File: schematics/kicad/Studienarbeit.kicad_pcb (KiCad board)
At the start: 2 copper layers, 73 x 73 mm, 84 parts, among them J2 Conn_01x18, J3 Conn_01x18, J4 Conn_01x01_Pin, J5 Conn_01x01_Pin, J6 Conn_01x01_Pin, J7 Conn_01x01_Pin, J9 SJ2-35853B-SMT-TR, U2 PCM5102, U3 MCP6001-OT, U4 MCP6001-OT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

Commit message: Last board updates before ordering.
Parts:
- removed CC_TPA711: 330uF, Capacitor_SMD:C_1206_3216Metric_Pad1.33x1.80mm_HandSolder
- added C_INPUT_TPA3: 10uF, Capacitor_SMD:C_1206_3216Metric_Pad1.33x1.80mm_HandSolder, F.Cu at (266.1, 77.5)
- C2_CPPS_PCM1, CA_PCM5102, CB_TPA1: footprint Capacitor_SMD:C_0805_2012Metric_Pad1.18x1.45mm_HandSolder -> Capacitor_SMD:C_1206_3216Metric_Pad1.33x1.80mm_HandSolder
- moved C1_CPPS_PCM1 1.17 mm to (235.8, 102.2)
- moved C2_CPPS_PCM1 0.88 mm to (230.4, 102.3)
- moved C1_DPS_PCM1 0.63 mm to (225.4, 101.5)
- moved C2_DPS_PCM1 0.60 mm to (221.8, 101.2)
- moved CG1_PCM5102 0.59 mm to (236.9, 89.2)
- moved CG2_PCM5102 0.59 mm to (234.6, 89.2)
- moved ROUTDACL1 0.59 mm to (236.9, 93.6)
- moved ROUTDACR1 0.59 mm to (234.6, 93.5)
- moved CB_TPA1 0.48 mm to (253.0, 70.2)
- moved C_SE/BTL_TPA1 0.40 mm to (254.2, 74.0)
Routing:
- net GND: track 90.4 -> 87.5 mm
- net +5V: track 247.2 -> 250.2 mm
- net /Vo+: track 25.6 -> 27.0 mm
- net /VNEG: track 5.05 -> 6.36 mm

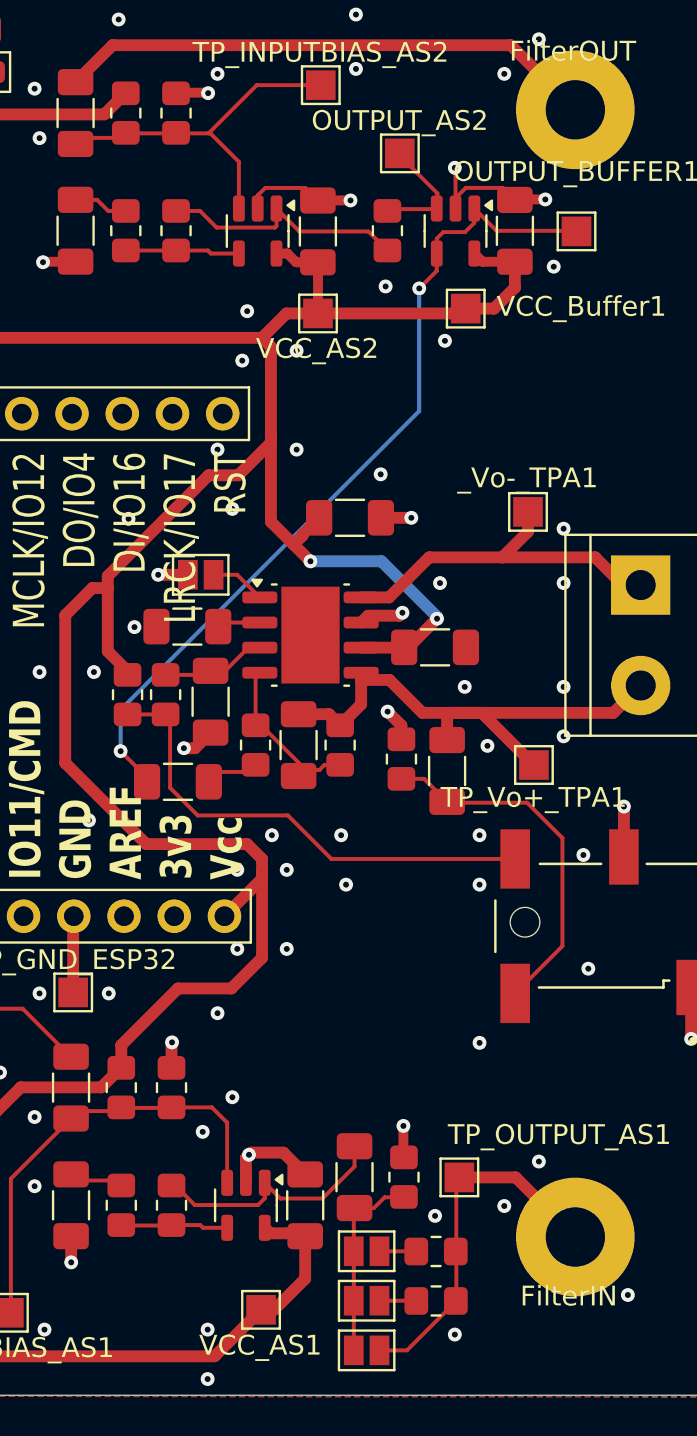
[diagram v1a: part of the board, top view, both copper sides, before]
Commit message: Updated MCP footprint and symbol
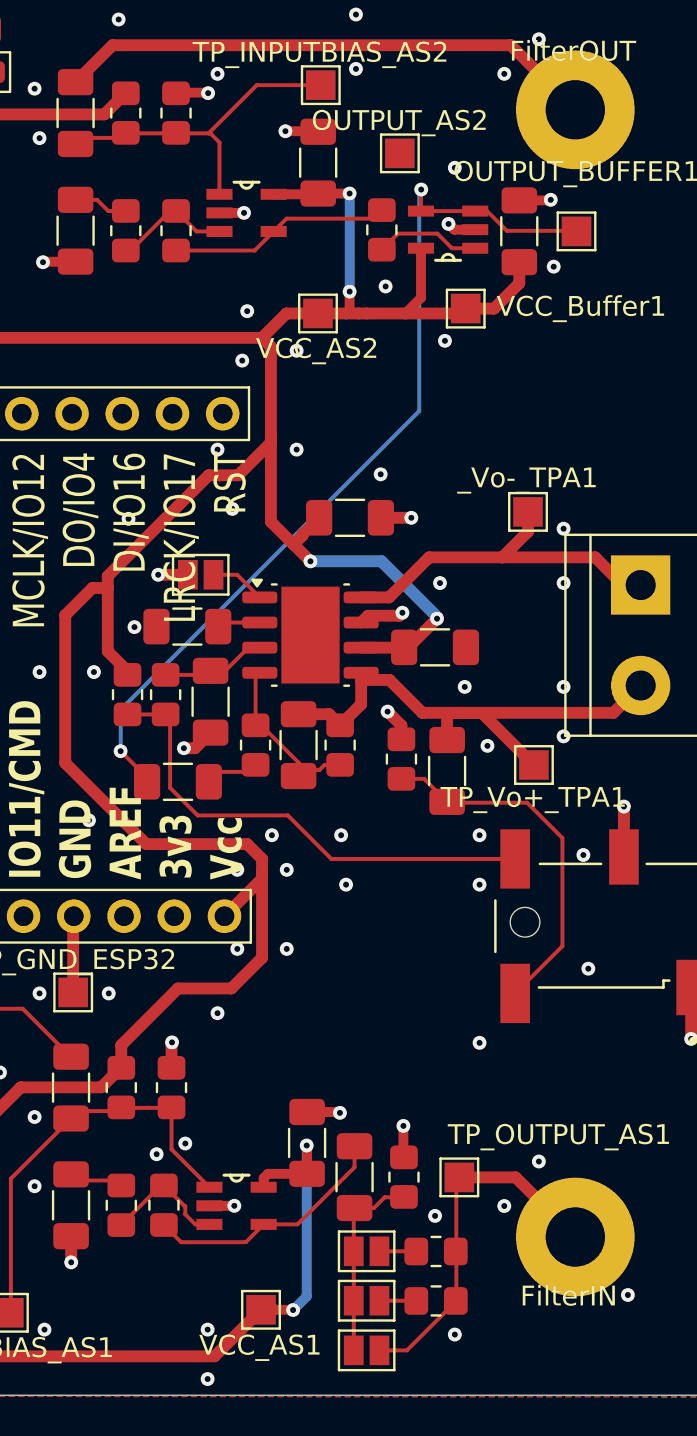
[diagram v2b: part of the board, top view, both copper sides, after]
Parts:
- removed U5: MCP6001, Package_TO_SOT_SMD:SOT-23-5
- added U1: MCP6001-OT, MCP6001UT:SOT95P270X145-5N, F.Cu at (256.0, 49.3)
- U3, U4: footprint Package_TO_SOT_SMD:SOT-23-5 -> MCP6001UT:SOT95P270X145-5N
- moved U3 9.63 mm to (266.2, 50.1), turned to 180 degrees
- moved C_COUPLING_AMPSTAGE3 3.48 mm to (259.6, 46.7)
- moved C_COUPLING_AMPSTAGE2 3.16 mm to (259.0, 96.3)
- moved U4 0.48 mm to (255.5, 99.5), turned to 0 degrees
- moved RF1 0.38 mm to (251.8, 99.5), turned to -90 degrees
- moved DEBUG1 0.28 mm to (262.8, 50.1), turned to -90 degrees
- moved C_COUPLING_AMPSTAGE4 0.22 mm to (269.8, 50.2)
- turned RF2 to -90 degrees
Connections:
- C_IN_AMPSTAGE1 pad 2: Net-(U3-+) -> Net-(U1-+)
- DEBUG1 pad 2: Net-(DEBUG1-Pad2) -> Net-(U3-+)
- R3 pad 1: Net-(U3-+) -> Net-(U1-+)
- R4 pad 1: Net-(U3-+) -> Net-(U1-+)
- RF2 pad 1: Net-(U3--) -> Net-(U1--)
- RG2 pad 2: Net-(U3--) -> Net-(U1--)
- TP_INPUTBIAS_AS2 pad 1: Net-(U3-+) -> Net-(U1-+)
- U3 pad 1: Net-(DEBUG1-Pad1) -> Net-(U3-+)
- U3 pad 3: Net-(U3-+) -> /BUFFEROUT
- U3 pad 4: Net-(U3--) -> /BUFFEROUT
- U4 pad 1: Net-(C_COUPLING_AMPSTAGE1-Pad2) -> Net-(U4-+)
- U4 pad 3: Net-(U4-+) -> Net-(U4--)
- U4 pad 4: Net-(U4--) -> Net-(C_COUPLING_AMPSTAGE1-Pad2)
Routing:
- net Net-(U1-+): track 0.00 -> 16.2 mm
- net +5V: track 250.2 -> 264.8 mm, vias 2 -> 6
- net Net-(U3-+): track 17.4 -> 5.36 mm
- net GND: track 87.5 -> 77.6 mm, vias 145 -> 148
- net Net-(U1--): track 0.00 -> 5.99 mm
- net Net-(U3--): track 5.78 -> 0.00 mm
- net Net-(DEBUG1-Pad2): track 5.04 -> 0.00 mm
- net /BUFFEROUT: track 43.0 -> 45.9 mm
- net Net-(DEBUG1-Pad1): track 12.8 -> 11.3 mm
- net Net-(U4-+): track 21.8 -> 20.5 mm
- net Net-(U4--): track 5.39 -> 6.35 mm

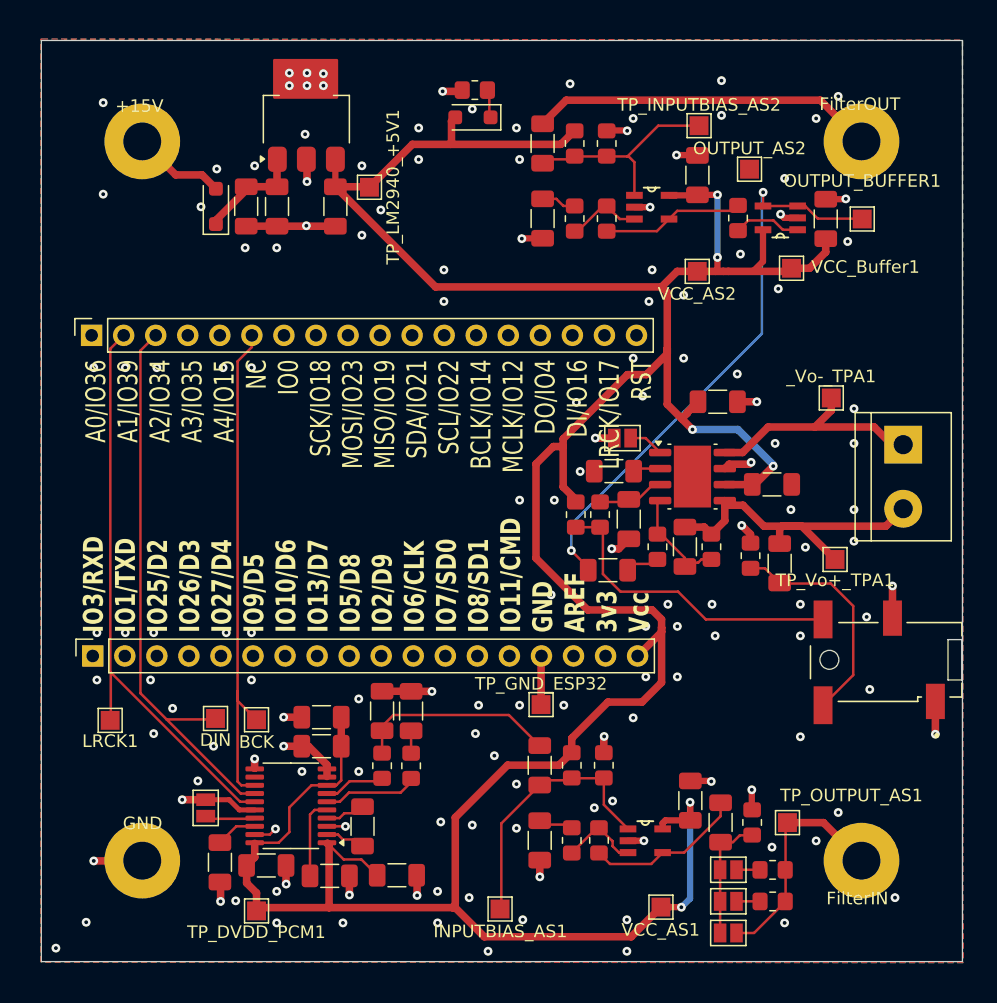
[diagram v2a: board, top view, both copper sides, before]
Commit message: Re-Added copper Layer
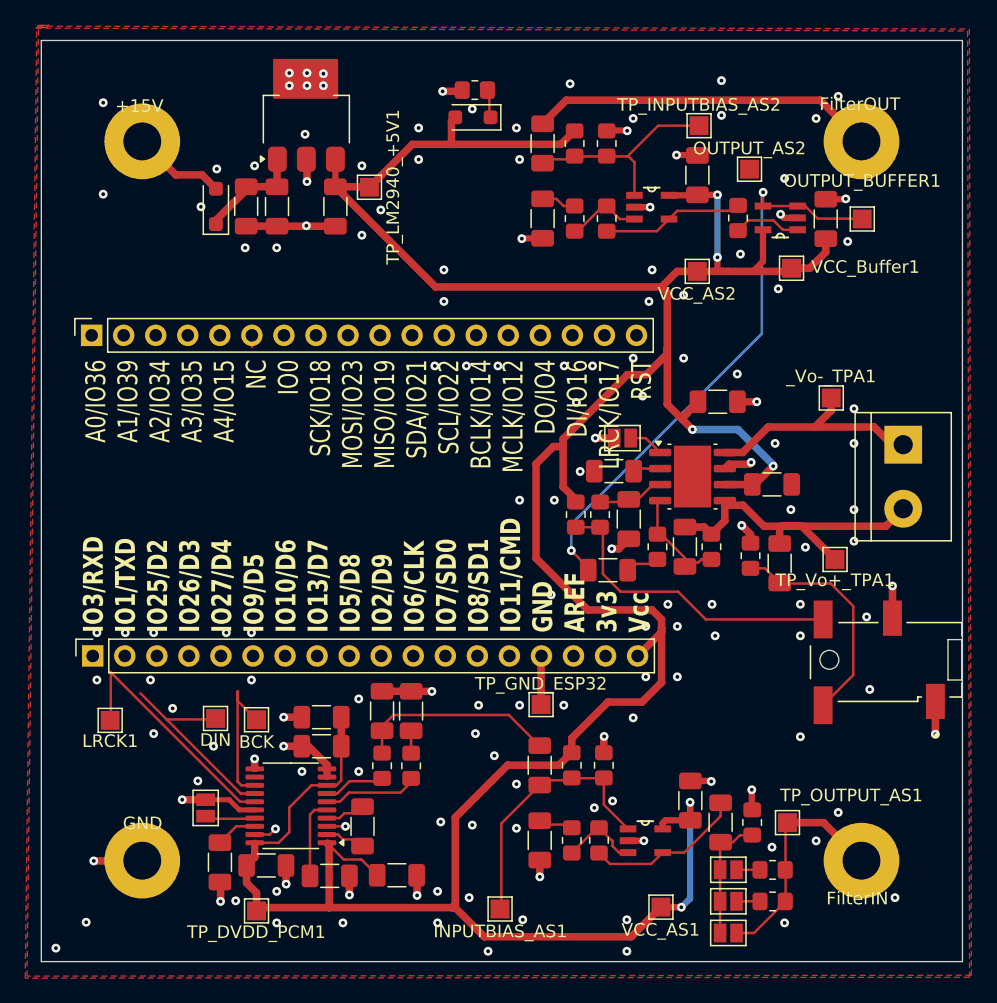
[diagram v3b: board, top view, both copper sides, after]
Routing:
- net /DIN: track 45.0 -> 16.1 mm
- net /BCK: track 40.2 -> 12.4 mm
- net /LRCK: track 46.6 -> 19.5 mm
- removed copper zone on B.Cu, net GND
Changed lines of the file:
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@@
 	)
 	(via
-		(at 216.75 62)
+		(at 243.78 61.86)
 		(size 0.7)
 		(drill 0.3)
@@
 	)
 	(via
-		(at 211.75 62)
+		(at 238.78 61.86)
 		(size 0.7)
 		(drill 0.3)
@@
 	)
 	(via
-		(at 214.25 62)
+		(at 241.28 61.86)
 		(size 0.7)
 		(drill 0.3)
@@
 	)
 	(via
-		(at 222 62)
+		(at 249.03 61.86)
 		(size 0.7)
 		(drill 0.3)
@@
 	)
 	(via
-		(at 224.25 62)
+		(at 251.28 61.86)
 		(size 0.7)
 		(drill 0.3)
@@
 	)
 	(segment
-		(start 224.282 60.368)
-		(end 223.15 61.5)
-		(width 0.2)
-		(layer "F.Cu")
-		(net 25)
-	)
-	(segment
 		(start 223.44725 95.09725)
 		(end 224.5075 95.09725)
@@
 	)
 	(segment
-		(start 223.15 61.5)
-		(end 223.15 87.65)
-		(width 0.2)
-		(layer "F.Cu")
-		(net 25)
-	)
-	(segment
 		(start 223.15 87.65)
 		(end 223.15 94.8)
@@
 	)
 	(segment
-		(start 216.662 59.436)
-		(end 215.45 60.648)
-		(width 0.2)
-		(layer "F.Cu")
-		(net 26)
-	)
-	(segment
-		(start 215.45 60.648)
-		(end 215.45 87.8)
-		(width 0.2)
-		(layer "F.Cu")
-		(net 26)
-	)
-	(segment
 		(start 223.39725 95.74725)
 		(end 224.5075 95.74725)
@@
 	)
 	(segment
-		(start 213.062 60.496)
-		(end 213.062 86.112)
-		(width 0.2)
-		(layer "F.Cu")
-		(net 62)
-	)
-	(segment
 		(start 213.1 89.9)
 		(end 213.1 86.15)
@@
 	)
 	(segment
-		(start 214.122 59.436)
-		(end 213.062 60.496)
-		(width 0.2)
-		(layer "F.Cu")
-		(net 62)
-	)
-	(segment
 		(start 262.69 104.29)
 		(end 264.5175 104.29)
@@
 		(net 1)
 		(net_name "GND")
-		(layers "F&B.Cu")
+		(layer "F.Cu")
+		(hatch edge 0.5)
+		(connect_pads
+			(clearance 0.5)
+		)
+		(min_thickness 0.25)
+		(filled_areas_thickness no)
+		(fill yes
+			(thermal_gap 0.5)
+			(thermal_bridge_width 0.5)
+		)
+		(polygon
+			(pts
+				(xy 207.302975 34.930488) (xy 281.142975 35.160488) (xy 281.302975 110.150488) (xy 206.462975 110.220488)
+				(xy 207.372975 34.860488) (xy 208.212975 34.860488)
+			)
+		)
+	)
+	(zone
+		(net 1)
+		(net_name "GND")
+		(layer "F.Cu")
+		(hatch edge 0.5)
+		(connect_pads
+			(clearance 0.5)
+		)
+		(min_thickness 0.25)
+		(filled_areas_thickness no)
+		(fill yes
+			(thermal_gap 0.5)
+			(thermal_bridge_width 0.5)
+		)
+		(polygon
+			(pts
+				(xy 207.16 35.09) (xy 281 35.32) (xy 281.16 110.31) (xy 206.32 110.38) (xy 207.23 35.02) (xy 208.07 35.02)
+			)
+		)
+	)
+	(zone
+		(net 0)
+		(net_name "")
+		(layer "Edge.Cuts")
 		(hatch edge 0.5)
 		(connect_pads
@@
 			(thermal_gap 0.5)
 			(thermal_bridge_width 0.5)
-			(island_removal_mode 2)
-			(island_area_min 4)
 		)
 		(polygon
 			(pts
-				(xy 207.65 35.95) (xy 280.6 36.05) (xy 280.65 109.15) (xy 207.55 109.1) (xy 207.55 35.95)
+				(xy 207.594 36.068) (xy 280.594 36.068) (xy 280.594 109.068) (xy 207.594 109.068)
 			)
 		)

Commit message: Updated output pins of the ESP
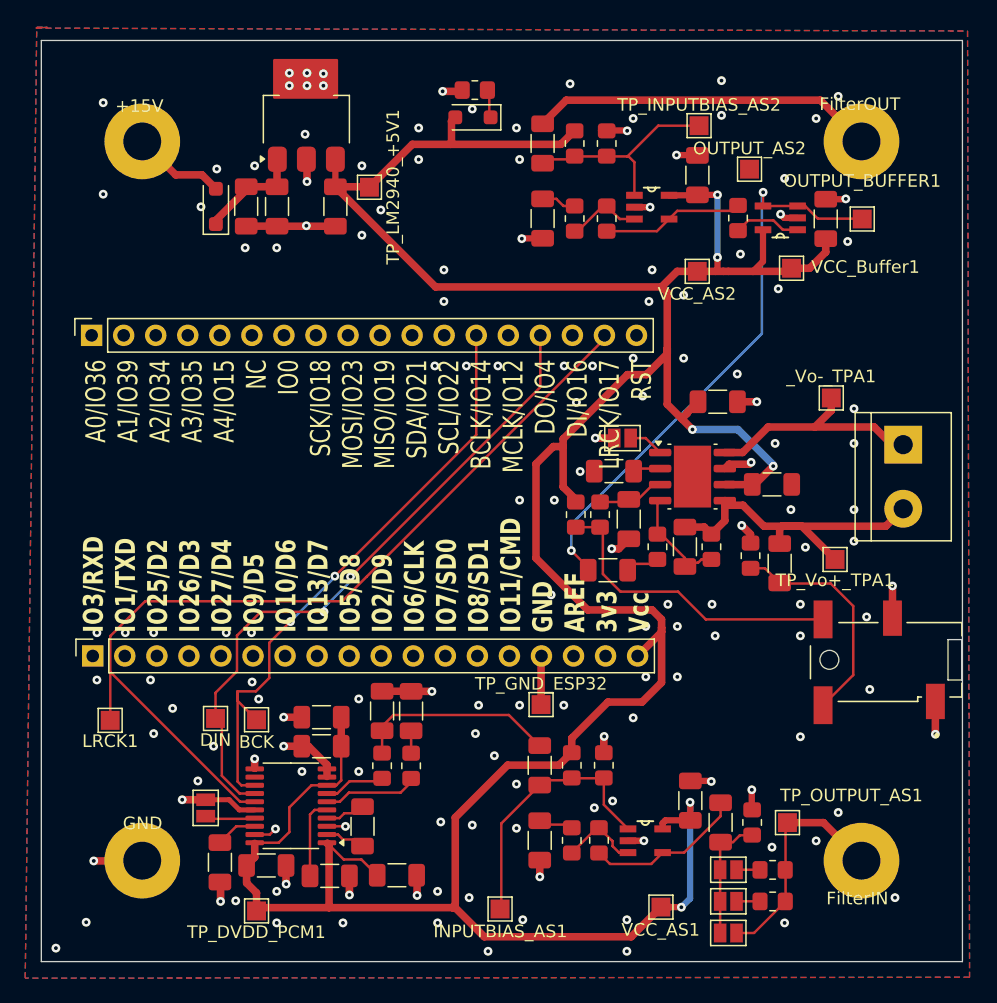
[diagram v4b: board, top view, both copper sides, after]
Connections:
- J3 pad 13: unconnected-(J3-Pin_13-Pad13) -> /BCK
- J3 pad 15: unconnected-(J3-Pin_15-Pad15) -> /DIN
- J3 pad 17: unconnected-(J3-Pin_17-Pad17) -> /LRCK
- J3 pad 2: /LRCK -> unconnected-(J3-Pin_2-Pad2)
- J3 pad 3: /DIN -> unconnected-(J3-Pin_3-Pad3)
- J3 pad 6: /BCK -> unconnected-(J3-Pin_6-Pad6)
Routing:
- net /LRCK: track 19.5 -> 72.1 mm
- net /BCK: track 12.4 -> 48.4 mm, vias 0 -> 2
- net /DIN: track 16.1 -> 51.8 mm, vias 0 -> 2
- net GND: vias 148 -> 149
- added copper zone on B.Cu, net GND

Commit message: Replaced footprint with the one from the prof.
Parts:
- added C_INPUT_RT1: 22uF, Capacitor_SMD:C_1206_3216Metric_Pad1.33x1.80mm_HandSolder, F.Cu at (217.0, 94.4)
- added C_INPUT_RT9080: 1uF, Capacitor_SMD:C_1206_3216Metric_Pad1.33x1.80mm_HandSolder, F.Cu at (210.3, 94.1)
- added U5: RT9080-33GJ5, RT9080-33GJ5:TSOT-23-5_RIT-L, F.Cu at (213.7, 93.4)
- moved LRCK1 5.10 mm to (218.2, 89.8)
- moved TP_DVDD_PCM1 0.80 mm to (224.3, 105.8)
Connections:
- C1_APS_PCM5102 pad 1: +5V -> +3v3
- C1_CPPS_PCM1 pad 2: +5V -> +3v3
- C1_DPS_PCM1 pad 2: +5V -> +3v3
- C2_APS_PCM5102 pad 2: +5V -> +3v3
- TP_DVDD_PCM1 pad 1: +5V -> +3v3
- U2 pad 1: +5V -> +3v3
- U2 pad 20: +5V -> +3v3
- U2 pad 8: +5V -> +3v3
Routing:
- net +3v3: track 0.00 -> 57.6 mm
- net /LRCK: track 72.1 -> 59.3 mm
- net +5V: track 264.8 -> 269.3 mm
- net GND: track 77.6 -> 78.2 mm, vias 149 -> 148
